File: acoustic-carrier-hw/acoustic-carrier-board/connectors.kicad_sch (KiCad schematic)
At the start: 5 parts, among them IC1 ECP5-BGA256, Y2 Crystal Oscillator

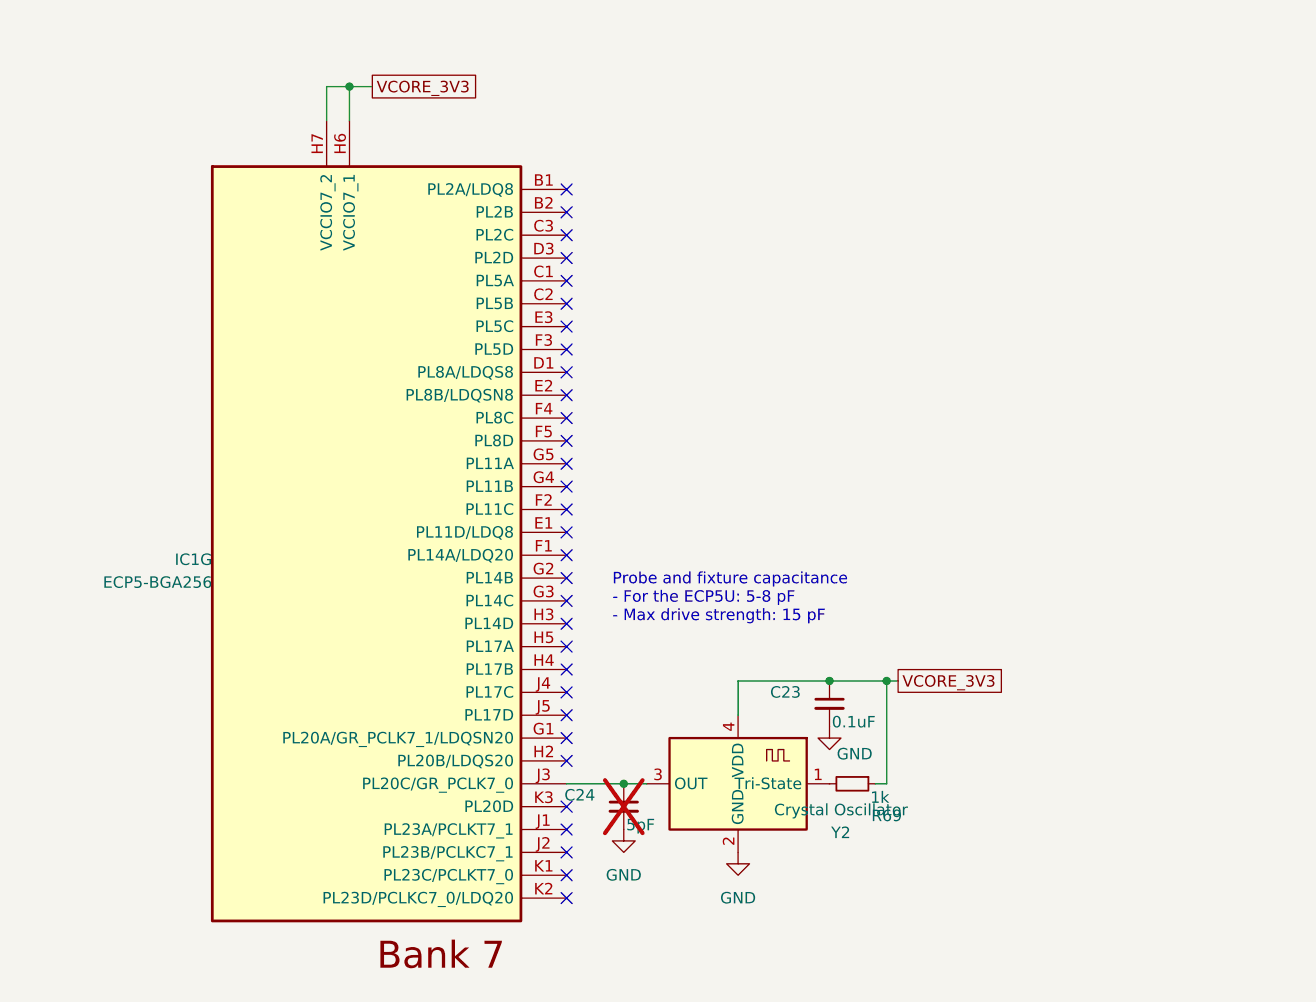
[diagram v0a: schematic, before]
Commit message: [carrier] Added hierarchical labels
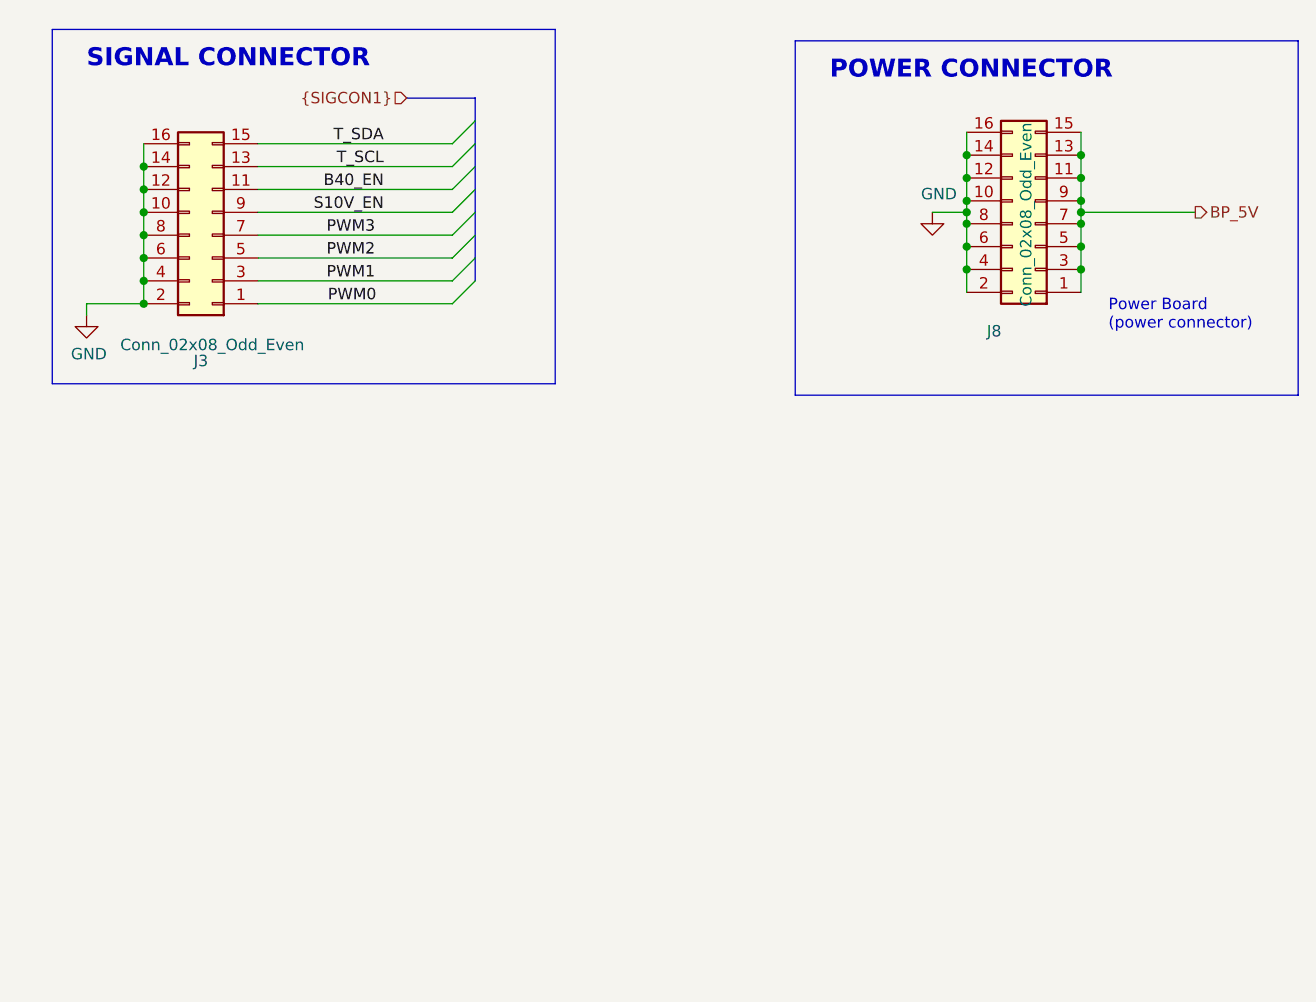
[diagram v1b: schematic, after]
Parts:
- removed C23: 0.1uF, Capacitor_SMD:C_0402_1005Metric, symbol Device:C_Small
- removed C24: 5pF, Capacitor_SMD:C_0603_1608Metric, symbol Device:C_Small
- removed IC1: ECP5-BGA256, iw-fpga_mcu:BGA256C80P16X16_1400X1400X170, symbol iw-fpga_mcu:ECP5-BGA256
- removed R69: 1k, Resistor_SMD:R_0603_1608Metric, symbol Device:R_Small
- removed Y2: Crystal Oscillator, Crystal:Crystal_SMD_3225-4Pin_3.2x2.5mm, symbol Oscillator:ASCO
- added J3, J8: Conn_02x08_Odd_Even, Connector_PinSocket_2.54mm:PinSocket_2x08_P2.54mm_Horizontal, symbol Connector_Generic:Conn_02x08_Odd_Even
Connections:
- net GND: now also J3.10 (Pin_10), J3.12 (Pin_12), J3.14 (Pin_14), J3.16 (Pin_16), J3.2 (Pin_2), J3.4 (Pin_4), J3.6 (Pin_6), J3.8 (Pin_8), J8.10 (Pin_10), J8.12 (Pin_12), J8.14 (Pin_14), J8.16 (Pin_16), J8.2 (Pin_2), J8.4 (Pin_4), J8.6 (Pin_6), J8.8 (Pin_8)
- new net B40_EN: J3.11 (Pin_11)
- new net BP_5V: J8.1 (Pin_1), J8.11 (Pin_11), J8.13 (Pin_13), J8.15 (Pin_15), J8.3 (Pin_3), J8.5 (Pin_5), J8.7 (Pin_7), J8.9 (Pin_9)
- new net PWM0: J3.1 (Pin_1)
- new net PWM1: J3.3 (Pin_3)
- new net PWM2: J3.5 (Pin_5)
- new net PWM3: J3.7 (Pin_7)
- new net S10V_EN: J3.9 (Pin_9)
- new net T_SCL: J3.13 (Pin_13)
- new net T_SDA: J3.15 (Pin_15)
- no-connect marks 31 -> 0
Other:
- note added: "POWER CONNECTOR"
- note added: "Power Board (power connector)"
- note added: "SIGNAL CONNECTOR"
- note removed: "Probe and fixture capacitance - For the ECP5U: 5-8 pF - Max drive strength: 15 pF"

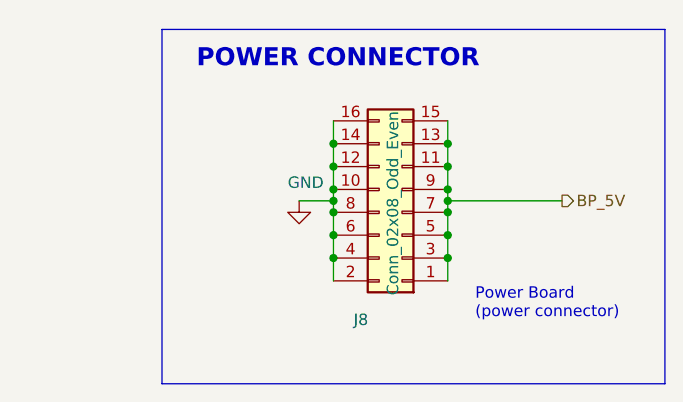
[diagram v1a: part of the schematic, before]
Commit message: [carrier] Added extra decoupling to ECP5U according to datasheet (next) perform page-wise checks, add testpoints
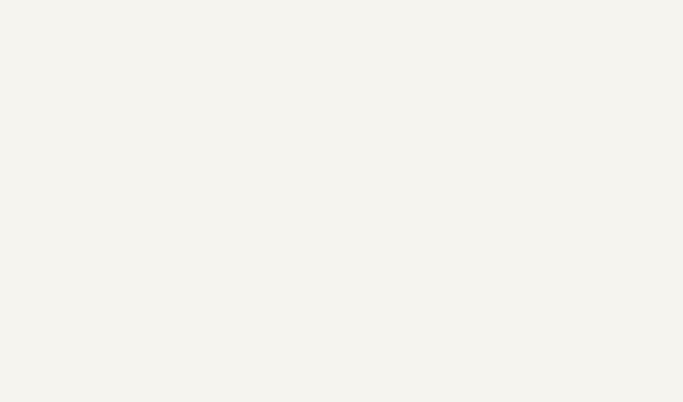
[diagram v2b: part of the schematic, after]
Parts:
- removed J8: Conn_02x08_Odd_Even, Connector_PinSocket_2.54mm:PinSocket_2x08_P2.54mm_Horizontal, symbol Connector_Generic:Conn_02x08_Odd_Even
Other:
- note removed: "POWER CONNECTOR"
- note removed: "Power Board (power connector)"

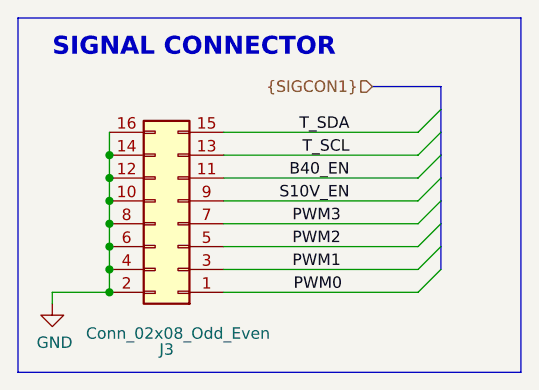
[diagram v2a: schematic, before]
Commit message: [carrier] Added testpoints
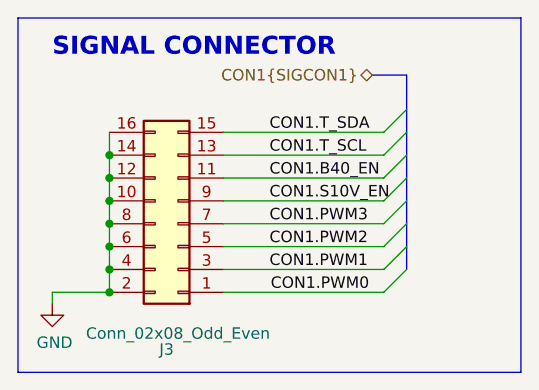
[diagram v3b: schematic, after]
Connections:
- net B40_EN renamed CON1.B40_EN
- net PWM0 renamed CON1.PWM0
- net PWM1 renamed CON1.PWM1
- net PWM2 renamed CON1.PWM2
- net PWM3 renamed CON1.PWM3
- net S10V_EN renamed CON1.S10V_EN
- net T_SCL renamed CON1.T_SCL
- net T_SDA renamed CON1.T_SDA

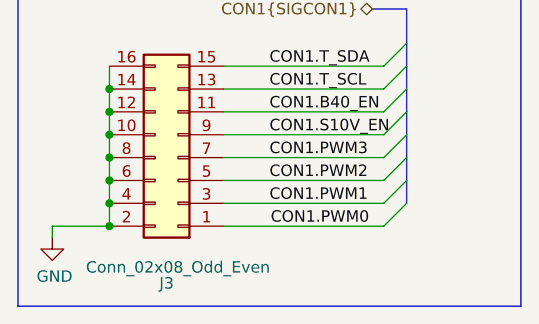
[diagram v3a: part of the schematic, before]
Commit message: [carrier] Finished rough layout, p (put together according to component category
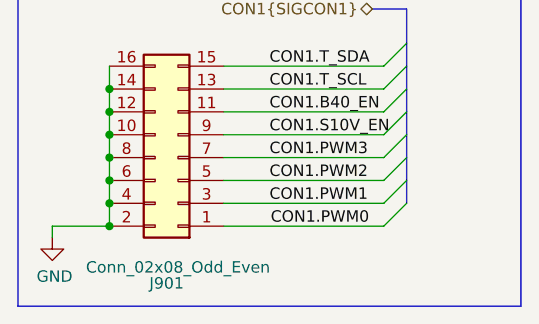
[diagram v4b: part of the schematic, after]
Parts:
- renumbered J3 to J901
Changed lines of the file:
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@@
 		(on_board yes)
 		(dnp no)
-		(property "Reference" "J3"
+		(property "Reference" "J901"
 			(at 40.64 72.39 0)
 			(effects
@@
 			(project "acoustic-carrier-board"
 				(path "/25b015c9-ab13-4427-b72c-b6f348597100/bc102b0c-2088-41b9-b570-4eb098131c8b"
-					(reference "J3")
+					(reference "J901")
 					(unit 1)
 				)
@@
 		(on_board yes)
 		(dnp no)
-		(property "Reference" "#PWR024"
+		(property "Reference" "#PWR0901"
 			(at 27.94 73.66 0)
 			(effects
@@
 			(project "acoustic-carrier-board"
 				(path "/25b015c9-ab13-4427-b72c-b6f348597100/bc102b0c-2088-41b9-b570-4eb098131c8b"
-					(reference "#PWR024")
+					(reference "#PWR0901")
 					(unit 1)
 				)

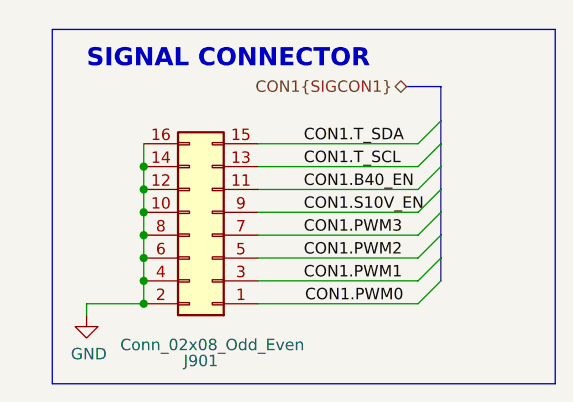
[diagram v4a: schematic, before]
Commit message: [carrier] Layout more or less complete (next) think about adding 6x2 connectors, and add extra pin signals to the connector for testing
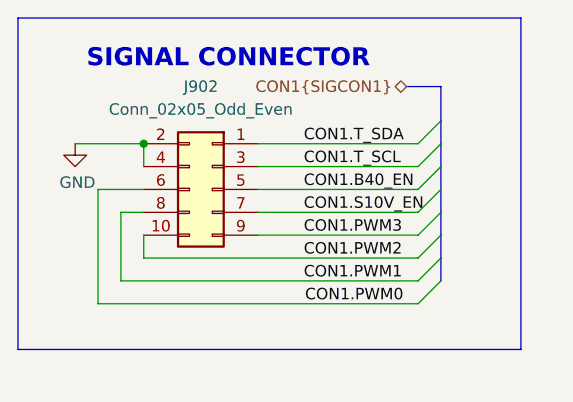
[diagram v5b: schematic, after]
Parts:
- removed J901: Conn_02x08_Odd_Even, Connector_PinSocket_2.54mm:PinSocket_2x08_P2.54mm_Horizontal, symbol Connector_Generic:Conn_02x08_Odd_Even
- added J902: Conn_02x05_Odd_Even, Connector_PinSocket_2.54mm:PinSocket_2x05_P2.54mm_Horizontal, symbol Connector_Generic:Conn_02x05_Odd_Even
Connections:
- net CON1.B40_EN: now also J902.5 (Pin_5)
- net CON1.PWM0: now also J902.6 (Pin_6)
- net CON1.PWM1: now also J902.8 (Pin_8)
- net CON1.PWM2: now also J902.10 (Pin_10)
- net CON1.PWM3: now also J902.9 (Pin_9)
- net CON1.S10V_EN: now also J902.7 (Pin_7)
- net CON1.T_SCL: now also J902.3 (Pin_3)
- net CON1.T_SDA: now also J902.1 (Pin_1)
- net GND: now also J902.2 (Pin_2), J902.4 (Pin_4)

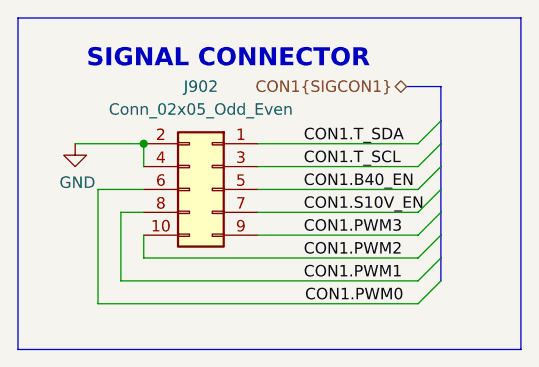
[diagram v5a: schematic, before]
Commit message: [carrier] Added testpoints to rj45, added 6xx2 connectors (next) start routing the digital section
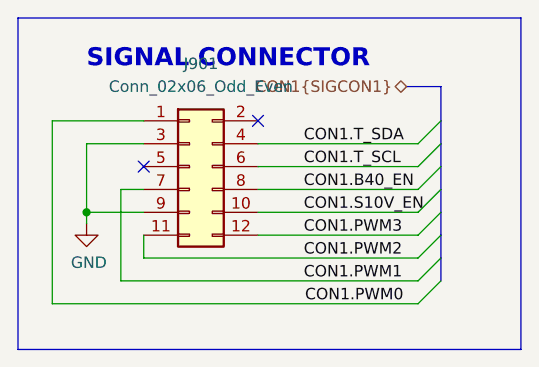
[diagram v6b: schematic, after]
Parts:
- removed J902: Conn_02x05_Odd_Even, Connector_PinSocket_2.54mm:PinSocket_2x05_P2.54mm_Horizontal, symbol Connector_Generic:Conn_02x05_Odd_Even
- added J901: Conn_02x06_Odd_Even, Connector_PinSocket_2.54mm:PinSocket_2x06_P2.54mm_Horizontal, symbol Connector_Generic:Conn_02x06_Odd_Even
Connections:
- net CON1.B40_EN: now also J901.8 (Pin_8)
- net CON1.PWM0: now also J901.1 (Pin_1)
- net CON1.PWM1: now also J901.7 (Pin_7)
- net CON1.PWM2: now also J901.11 (Pin_11)
- net CON1.PWM3: now also J901.12 (Pin_12)
- net CON1.S10V_EN: now also J901.10 (Pin_10)
- net CON1.T_SCL: now also J901.6 (Pin_6)
- net CON1.T_SDA: now also J901.4 (Pin_4)
- net GND: now also J901.3 (Pin_3), J901.9 (Pin_9)
- no-connect marks 0 -> 2
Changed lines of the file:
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@@
 	)
 	(junction
-		(at 34.29 48.26)
+		(at 27.94 55.88)
 		(diameter 0)
 		(color 0 0 0 0)
 	)
+	(no_connect
+		(at 46.99 45.72)
+	)
+	(no_connect
+		(at 34.29 50.8)
+	)
 	(bus_entry
 		(at 64.77 58.42)
@@
 		)
 	)
-	(wire
-		(pts
-			(xy 31.75 55.88) (xy 34.29 55.88)
-		)
-		(stroke
-			(width 0)
-			(type default)
-		)
-	)
 	(bus
 		(pts
@@
 		)
 	)
+	(wire
+		(pts
+			(xy 27.94 55.88) (xy 34.29 55.88)
+		)
+		(stroke
+			(width 0)
+			(type default)
+		)
+	)
 	(bus
 		(pts
@@
 		)
 	)
-	(wire
-		(pts
-			(xy 26.67 48.26) (xy 34.29 48.26)
-		)
-		(stroke
-			(width 0)
-			(type default)
-		)
-	)
 	(bus
 		(pts
@@
 		)
 	)
+	(wire
+		(pts
+			(xy 27.94 55.88) (xy 27.94 48.26)
+		)
+		(stroke
+			(width 0)
+			(type default)
+		)
+	)
+	(wire
+		(pts
+			(xy 24.13 45.72) (xy 34.29 45.72)
+		)
+		(stroke
+			(width 0)
+			(type default)
+		)
+	)
 	(bus
 		(pts
@@
 	(wire
 		(pts
-			(xy 34.29 50.8) (xy 34.29 48.26)
-		)
-		(stroke
-			(width 0)
-			(type default)
-		)
-	)
-	(wire
-		(pts
 			(xy 34.29 60.96) (xy 34.29 58.42)
 		)
@@
 	(wire
 		(pts
-			(xy 29.21 53.34) (xy 34.29 53.34)
+			(xy 27.94 57.15) (xy 27.94 55.88)
 		)
 		(stroke
@@
 	(wire
 		(pts
+			(xy 27.94 48.26) (xy 34.29 48.26)
+		)
+		(stroke
+			(width 0)
+			(type default)
+		)
+	)
+	(wire
+		(pts
+			(xy 34.29 53.34) (xy 31.75 53.34)
+		)
+		(stroke
+			(width 0)
+			(type default)
+		)
+	)
+	(wire
+		(pts
 			(xy 64.77 58.42) (xy 46.99 58.42)
 		)
@@
 	(wire
 		(pts
-			(xy 29.21 66.04) (xy 64.77 66.04)
+			(xy 24.13 66.04) (xy 64.77 66.04)
 		)
 		(stroke
@@
 	(wire
 		(pts
+			(xy 24.13 45.72) (xy 24.13 66.04)
+		)
+		(stroke
+			(width 0)
+			(type default)
+		)
+	)
+	(wire
+		(pts
 			(xy 64.77 50.8) (xy 46.99 50.8)
 		)
@@
 		)
 	)
-	(wire
-		(pts
-			(xy 29.21 66.04) (xy 29.21 53.34)
-		)
-		(stroke
-			(width 0)
-			(type default)
-		)
-	)
 	(bus
 		(pts
@@
 	(wire
 		(pts
-			(xy 31.75 63.5) (xy 31.75 55.88)
+			(xy 31.75 53.34) (xy 31.75 63.5)
 		)
 		(stroke
@@
 	)
 	(symbol
-		(lib_id "Connector_Generic:Conn_02x05_Odd_Even")
-		(at 41.91 53.34 0)
-		(mirror y)
+		(lib_id "Connector_Generic:Conn_02x06_Odd_Even")
+		(at 39.37 50.8 0)
 		(unit 1)
 		(exclude_from_sim no)
@@
 		(on_board yes)
 		(dnp no)
-		(property "Reference" "J902"
+		(fields_autoplaced yes)
+		(property "Reference" "J901"
+			(at 40.64 39.37 0)
+			(effects
+				(font
+					(size 1.27 1.27)
+				)
+			)
+		)
+		(property "Value" "Conn_02x06_Odd_Even"
 			(at 40.64 41.91 0)
 			(effects
@@
 			)
 		)
-		(property "Value" "Conn_02x05_Odd_Even"
-			(at 40.64 44.45 0)
-			(effects
-				(font
-					(size 1.27 1.27)
-				)
-			)
-		)
-		(property "Footprint" "Connector_PinSocket_2.54mm:PinSocket_2x05_P2.54mm_Horizontal"
-			(at 41.91 53.34 0)
-			(effects
-				(font
-					(size 1.27 1.27)
-				)
-				(hide yes)
-			)
-		)
-		(property "Datasheet" "https://jlcpcb.com/api/file/downloadByFileSystemAccessId/8588944816709242880"
-			(at 41.91 53.34 0)
-			(effects
-				(font
-					(size 1.27 1.27)
-				)
-				(hide yes)
-			)
-		)
-		(property "Description" "Generic connector, double row, 02x05, odd/even pin numbering scheme (row 1 odd numbers, row 2 even numbers), script generated (kicad-library-utils/schlib/autogen/connector/)"
-			(at 41.91 53.34 0)
-			(effects
-				(font
-					(size 1.27 1.27)
-				)
-				(hide yes)
-			)
-		)
-		(property "MPN" "PM254-2-05-W-8.5 "
-			(at 41.91 53.34 0)
-			(effects
-				(font
-					(size 1.27 1.27)
-				)
-				(hide yes)
-			)
-		)
-		(property "LPN" "C2897425"
-			(at 41.91 53.34 0)
-			(effects
-				(font
-					(size 1.27 1.27)
-				)
-				(hide yes)
-			)
+		(property "Footprint" "Connector_PinSocket_2.54mm:PinSocket_2x06_P2.54mm_Horizontal"
+			(at 39.37 50.8 0)
+			(effects
+				(font
+					(size 1.27 1.27)
+				)
+				(hide yes)
+			)
+		)
+		(property "Datasheet" "https://jlcpcb.com/api/file/downloadByFileSystemAccessId/8588945579091103744"
+			(at 39.37 50.8 0)
+			(effects
+				(font
+					(size 1.27 1.27)
+				)
+				(hide yes)
+			)
+		)
+		(property "Description" "Generic connector, double row, 02x06, odd/even pin numbering scheme (row 1 odd numbers, row 2 even numbers), script generated (kicad-library-utils/schlib/autogen/connector/)"
+			(at 39.37 50.8 0)
+			(effects
+				(font
+					(size 1.27 1.27)
+				)
+				(hide yes)
+			)
+		)
+		(property "LPN" "C2897426"
+			(at 39.37 50.8 0)
+			(effects
+				(font
+					(size 1.27 1.27)
+				)
+				(hide yes)
+			)
+		)
+		(property "MPN" "PM254-2-06-W-8.5 "
+			(at 39.37 50.8 0)
+			(effects
+				(font
+					(size 1.27 1.27)
+				)
+				(hide yes)
+			)
+		)
+		(pin "5"
+		)
+		(pin "11"
+		)
+		(pin "3"
+		)
+		(pin "7"
+		)
+		(pin "4"
+		)
+		(pin "10"
+		)
+		(pin "2"
+		)
+		(pin "9"
+		)
+		(pin "1"
 		)
 		(pin "6"
 		)
+		(pin "12"
+		)
 		(pin "8"
-		)
-		(pin "3"
-		)
-		(pin "10"
-		)
-		(pin "5"
-		)
-		(pin "1"
-		)
-		(pin "7"
-		)
-		(pin "4"
-		)
-		(pin "2"
-		)
-		(pin "9"
 		)
 		(instances
 			(project "acoustic-carrier-board"
 				(path "/25b015c9-ab13-4427-b72c-b6f348597100/bc102b0c-2088-41b9-b570-4eb098131c8b"
-					(reference "J902")
+					(reference "J901")
 					(unit 1)
 				)
@@
 	(symbol
 		(lib_id "power:GND")
-		(at 26.67 48.26 0)
+		(at 27.94 57.15 0)
 		(unit 1)
 		(exclude_from_sim no)
@@
 		(dnp no)
 		(property "Reference" "#PWR0901"
-			(at 26.67 54.61 0)
+			(at 27.94 63.5 0)
 			(effects
 				(font
@@
 		)
 		(property "Value" "GND"
-			(at 26.924 52.578 0)
+			(at 28.194 61.468 0)
 			(effects
 				(font
@@
 		)
 		(property "Footprint" ""
-			(at 26.67 48.26 0)
+			(at 27.94 57.15 0)
 			(effects
 				(font
@@
 		)
 		(property "Datasheet" ""
-			(at 26.67 48.26 0)
+			(at 27.94 57.15 0)
 			(effects
 				(font
@@
 		)
 		(property "Description" "Power symbol creates a global label with name \"GND\" , ground"
-			(at 26.67 48.26 0)
-			(effects
-				(font
+			(at 27.94 57.15 0)
+			(effects
+				(font
